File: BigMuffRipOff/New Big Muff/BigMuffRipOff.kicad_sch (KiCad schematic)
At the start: 9 parts, among them J2 NMJ6HFD2, J3 NMJ6HFD2, J4 2125201004, J6 2125201004, J7 2125201004

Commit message: new big muff completed
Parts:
- removed H1, H2, H3, H4: MountingHole, MountingHole:MountingHole_2.2mm_M2, symbol Mechanical:MountingHole
- removed J2, J3: NMJ6HFD2, Connector_Audio:Jack_6.35mm_Neutrik_NMJ6HFD2_Horizontal, symbol Connector_Audio:NMJ6HFD2
- removed J4, J6, J7: 2125201004, 284867-E-footprint:CONN_2125200001-SD_04_MOL, symbol Molex 4pin header vert:2125201004
- added J1: Conn_02x08_Odd_Even, Connector_PinHeader_2.54mm:PinHeader_2x08_P2.54mm_Horizontal, symbol Connector_Generic:Conn_02x08_Odd_Even
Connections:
- net GND: now also J1.13 (Pin_13), J1.14 (Pin_14), J1.3 (Pin_3), J1.4 (Pin_4)
- new net 12V: J1.1 (Pin_1), J1.2 (Pin_2)
- new net CS0: J1.11 (Pin_11)
- new net CS1: J1.7 (Pin_7)
- new net CS2: J1.5 (Pin_5)
- new net CS3: J1.9 (Pin_9)
- new net GUITAR_IN: J1.8 (Pin_8)
- new net GUITAR_OUT: J1.10 (Pin_10)
- new net MOSI: J1.12 (Pin_12)
- new net SPI_CLK: J1.6 (Pin_6)
- no-connect marks 3 -> 2
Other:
- removed sheet MCU
- sheet PowerStage ports: added none; removed LDO_EN
- note added: "Connector to Analog Controller"

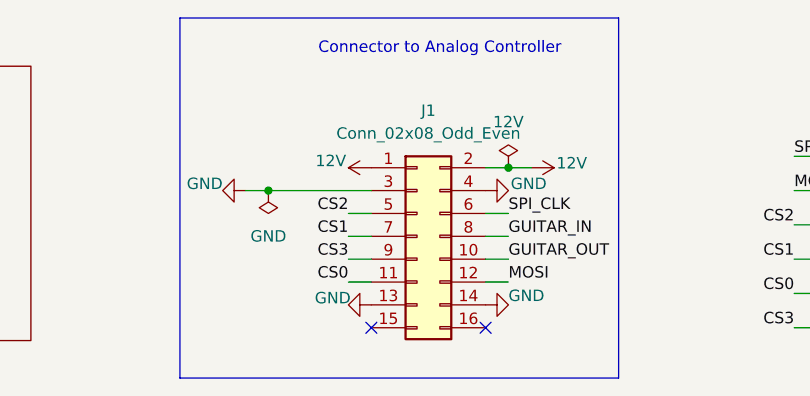
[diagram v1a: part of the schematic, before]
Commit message: connector for big muff updated
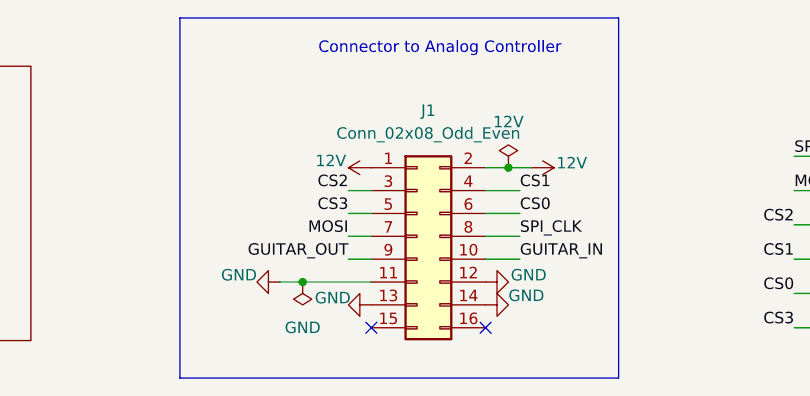
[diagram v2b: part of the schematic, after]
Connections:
- net CS0: now also J1.6 (Pin_6); no longer J1.11 (Pin_11)
- net CS1: now also J1.4 (Pin_4); no longer J1.7 (Pin_7)
- net CS2: now also J1.3 (Pin_3); no longer J1.5 (Pin_5)
- net CS3: now also J1.5 (Pin_5); no longer J1.9 (Pin_9)
- net GND: now also J1.11 (Pin_11), J1.12 (Pin_12); no longer J1.3 (Pin_3), J1.4 (Pin_4)
- net GUITAR_IN: now also J1.10 (Pin_10); no longer J1.8 (Pin_8)
- net GUITAR_OUT: now also J1.9 (Pin_9); no longer J1.10 (Pin_10)
- net MOSI: now also J1.7 (Pin_7); no longer J1.12 (Pin_12)
- net SPI_CLK: now also J1.8 (Pin_8); no longer J1.6 (Pin_6)

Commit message: big muff connector fixed i think?
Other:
- sheet Effect Stage ports: added Volume_CS_2, sustain_CS, tone_CS, volume_CS_1; removed CS_1, CS_2, CS_3, CS_4
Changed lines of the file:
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@@
-			)
-		)
-		(pin "CS_1" input
-			(at 203.2 97.79 180)
-			(effects
-				(font
-					(size 1.27 1.27)
-				)
-				(justify left)
-			)
-		)
-		(pin "CS_2" input
-			(at 203.2 101.6 180)
-			(effects
-				(font
-					(size 1.27 1.27)
-				)
-				(justify left)
-			)
-		)
-		(pin "CS_3" input
-			(at 203.2 105.41 180)
-			(effects
-				(font
-					(size 1.27 1.27)
-				)
-				(justify left)
 			)
 		)
@@
 			)
 		)
-		(pin "CS_4" input
-			(at 203.2 109.22 180)
+		(pin "SPI_MOSI" input
+			(at 203.2 93.98 180)
 			(effects
 				(font
@@
 			)
 		)
-		(pin "SPI_MOSI" input
-			(at 203.2 93.98 180)
+		(pin "sustain_CS" input
+			(at 203.2 97.79 180)
 			(effects
 				(font
+					(size 1.27 1.27)
+				)
+				(justify left)
+			)
+		)
+		(pin "tone_CS" input
+			(at 203.2 101.6 180)
+			(effects
+				(font
+					(size 1.27 1.27)
+				)
+				(justify left)
+			)
+		)
+		(pin "volume_CS_1" input
+			(at 203.2 105.41 180)
+			(effects
+				(font
+					(size 1.27 1.27)
+				)
+				(justify left)
+			)
+		)
+		(pin "Volume_CS_2" input
+			(at 203.2 109.22 180)
+			(effects
+				(font
